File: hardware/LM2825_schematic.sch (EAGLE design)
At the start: 4 parts, among them U1 ARDUINOR3-DIMENSION

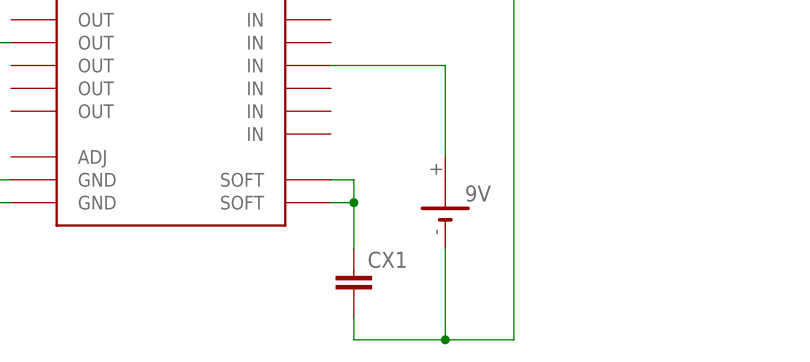
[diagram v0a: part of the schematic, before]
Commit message: updated soft-start capacitor to include value in schematic
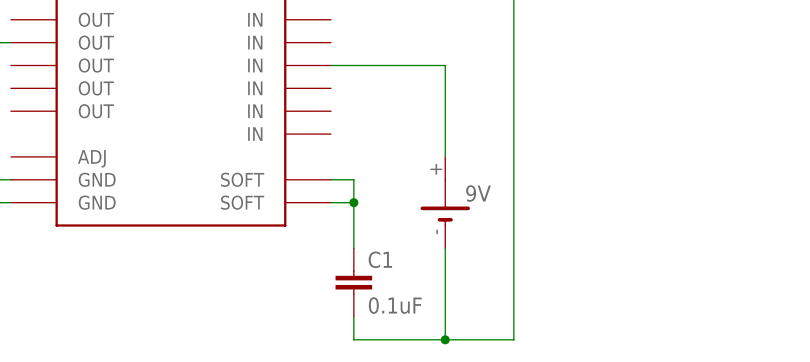
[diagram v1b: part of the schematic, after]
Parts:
- C1: value (none) -> 0.1uF
- renumbered CX1 to C1
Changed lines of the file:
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@@
 <part name="FRAME1" library="frames" deviceset="DOCFIELD" device=""/>
 <part name="U$5" library="BLE_sensor_pack_parts" deviceset="TI_LM2825" device=""/>
-<part name="CX1" library="rcl" deviceset="CX" device="XC10B5"/>
+<part name="C1" library="rcl" deviceset="CX" device="XC10B5" value="0.1uF"/>
 </parts>
 <sheets>
@@
 <instance part="FRAME1" gate="G$1" x="110.49" y="3.81"/>
 <instance part="U$5" gate="G$1" x="33.02" y="40.64"/>
-<instance part="CX1" gate="G$1" x="53.34" y="17.78"/>
+<instance part="C1" gate="G$1" x="53.34" y="17.78"/>
 </instances>
 <busses>
@@
 <wire x1="53.34" y1="50.8" x2="53.34" y2="60.96" width="0.1524" layer="91"/>
 <junction x="53.34" y="60.96"/>
-<pinref part="CX1" gate="G$1" pin="2"/>
+<pinref part="C1" gate="G$1" pin="2"/>
 <wire x1="53.34" y1="12.7" x2="53.34" y2="10.16" width="0.1524" layer="91"/>
 <wire x1="53.34" y1="10.16" x2="63.5" y2="10.16" width="0.1524" layer="91"/>
@@
 <net name="N$15" class="0">
 <segment>
-<pinref part="CX1" gate="G$1" pin="1"/>
+<pinref part="C1" gate="G$1" pin="1"/>
 <wire x1="53.34" y1="20.32" x2="53.34" y2="25.4" width="0.1524" layer="91"/>
 <pinref part="U$5" gate="G$1" pin="SOFT@14"/>
